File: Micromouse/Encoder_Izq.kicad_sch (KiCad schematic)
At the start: 6 parts, among them J10 AS5048_Izq, U4 AS5048B-HTSP

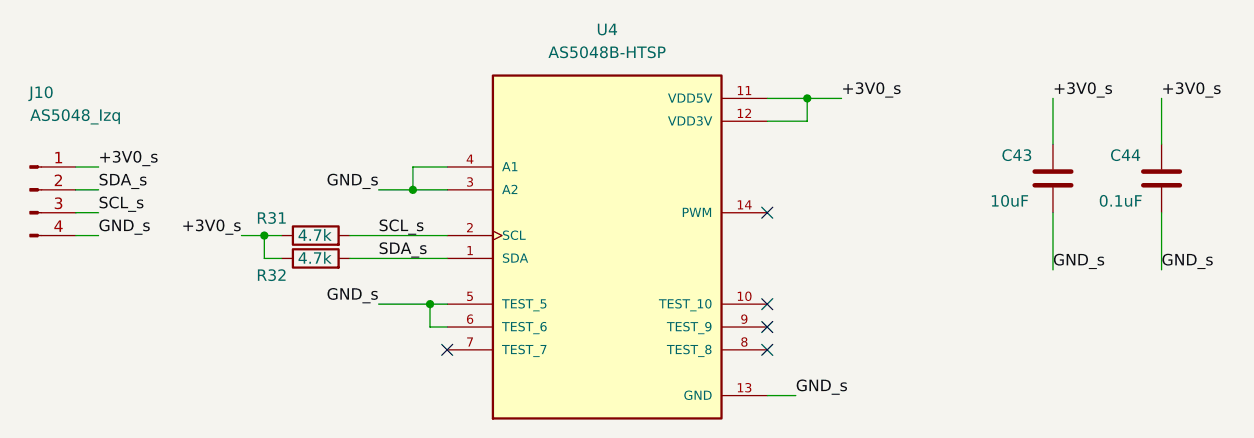
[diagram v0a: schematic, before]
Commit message: Red 3V0 cambiada a 3V3
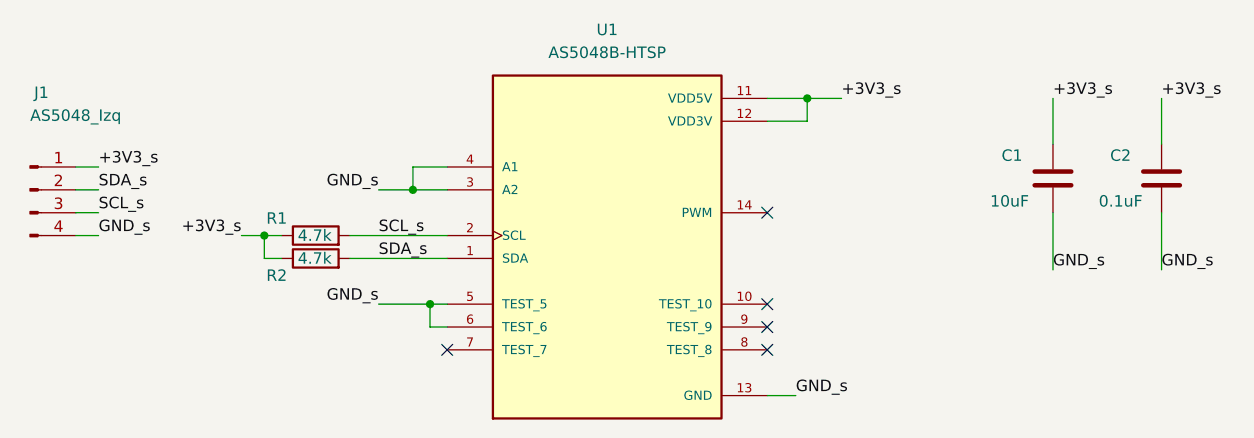
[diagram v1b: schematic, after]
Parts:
- renumbered C43 to C1, C44 to C2, J10 to J1, R31 to R1, R32 to R2, U4 to U1
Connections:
- net +3V0_s renamed +3V3_s
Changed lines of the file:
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@@
 		)
 	)
-	(label "+3V0_s"
+	(label "+3V3_s"
 		(at 110.49 105.41 180)
 		(effects
@@
 		)
 	)
-	(label "+3V0_s"
+	(label "+3V3_s"
 		(at 177.165 90.17 0)
 		(effects
@@
 		)
 	)
-	(label "+3V0_s"
+	(label "+3V3_s"
 		(at 200.66 90.17 0)
 		(effects
@@
 		)
 	)
-	(label "+3V0_s"
+	(label "+3V3_s"
 		(at 212.725 90.17 0)
 		(effects
@@
 		)
 	)
-	(label "+3V0_s"
+	(label "+3V3_s"
 		(at 94.615 97.79 0)
 		(effects
@@
 		(dnp no)
 		(fields_autoplaced yes)
-		(property "Reference" "U4"
+		(property "Reference" "U1"
 			(at 151.13 82.55 0)
 			(effects
@@
 		)
 		(instances
+			(project "Encoder_Izq"
+				(path "/7c92487d-362e-4a94-a0ea-71fb4eb52b74"
+					(reference "U1")
+					(unit 1)
+				)
+			)
 			(project ""
 				(path "/96b72c82-8e98-4b00-820e-849de0fa96c7/30dace89-d7fa-480e-aff2-f8c5b12c4053"
@@
 		(on_board yes)
 		(dnp no)
-		(property "Reference" "R31"
+		(property "Reference" "R1"
 			(at 115.57 103.505 90)
 			(effects
@@
 		)
 		(instances
+			(project "Encoder_Izq"
+				(path "/7c92487d-362e-4a94-a0ea-71fb4eb52b74"
+					(reference "R1")
+					(unit 1)
+				)
+			)
 			(project "Half-Size Micromouse"
 				(path "/96b72c82-8e98-4b00-820e-849de0fa96c7/30dace89-d7fa-480e-aff2-f8c5b12c4053"
@@
 		(on_board yes)
 		(dnp no)
-		(property "Reference" "J10"
+		(property "Reference" "J1"
 			(at 88.265 89.535 0)
 			(effects
@@
 		)
 		(instances
+			(project "Encoder_Izq"
+				(path "/7c92487d-362e-4a94-a0ea-71fb4eb52b74"
+					(reference "J1")
+					(unit 1)
+				)
+			)
 			(project "Half-Size Micromouse"
 				(path "/96b72c82-8e98-4b00-820e-849de0fa96c7/30dace89-d7fa-480e-aff2-f8c5b12c4053"
@@
 		(on_board yes)
 		(dnp no)
-		(property "Reference" "C44"
+		(property "Reference" "C2"
 			(at 207.01 96.52 0)
 			(effects
@@
 		)
 		(instances
+			(project "Encoder_Izq"
+				(path "/7c92487d-362e-4a94-a0ea-71fb4eb52b74"
+					(reference "C2")
+					(unit 1)
+				)
+			)
 			(project "Half-Size Micromouse"
 				(path "/96b72c82-8e98-4b00-820e-849de0fa96c7/30dace89-d7fa-480e-aff2-f8c5b12c4053"
@@
 		(on_board yes)
 		(dnp no)
-		(property "Reference" "R32"
+		(property "Reference" "R2"
 			(at 115.57 109.855 90)
 			(effects
@@
 		)
 		(instances
+			(project "Encoder_Izq"
+				(path "/7c92487d-362e-4a94-a0ea-71fb4eb52b74"
+					(reference "R2")
+					(unit 1)
+				)
+			)
 			(project "Half-Size Micromouse"
 				(path "/96b72c82-8e98-4b00-820e-849de0fa96c7/30dace89-d7fa-480e-aff2-f8c5b12c4053"
@@
 		(on_board yes)
 		(dnp no)
-		(property "Reference" "C43"
+		(property "Reference" "C1"
 			(at 194.945 96.52 0)
 			(effects
@@
 		)
 		(instances
+			(project "Encoder_Izq"
+				(path "/7c92487d-362e-4a94-a0ea-71fb4eb52b74"
+					(reference "C1")
+					(unit 1)
+				)
+			)
 			(project "Half-Size Micromouse"
 				(path "/96b72c82-8e98-4b00-820e-849de0fa96c7/30dace89-d7fa-480e-aff2-f8c5b12c4053"
@@
 		)
 	)
+	(sheet_instances
+		(path "/"
+			(page "1")
+		)
+	)
+	(embedded_fonts no)
 )
